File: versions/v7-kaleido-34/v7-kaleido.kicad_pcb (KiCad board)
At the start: 4 copper layers, 138.1 x 104.6 mm, 140 parts, among them J1 USB_C_Receptacle_USB2.0, J10 AXT-310124, J11 THD2528-11SD-GF, J12 SM04B-SRSS-TB_LF__SN_, J2 EXTENSION_HEADER, J3 USB_HDR, J4 Conn_01x08_Pin, J5 CONN_BAT, J6 FH34SRJ-6S-0.5SH_99_, J7 ESP_HDR, J8 ESP_XTR_HDR, J9 Conn_01x08_Pin, Q1 AO3401A, Q3 MMBT3904, Q4 MMBT3904, U1 RT9080-33GJ5, U10 ED060XC5, U11 TP4056, U12 RY3730, U2 PCA9535PW, U3 RSL48_4P4X4P4, U4 USBLC6-2P6, U5 XC6206PxxxMR, U6 RY3730, U7 PCF8563T, U8 ESP32-S3-WROOM-1, U9 CH340C, Y1 32.768K

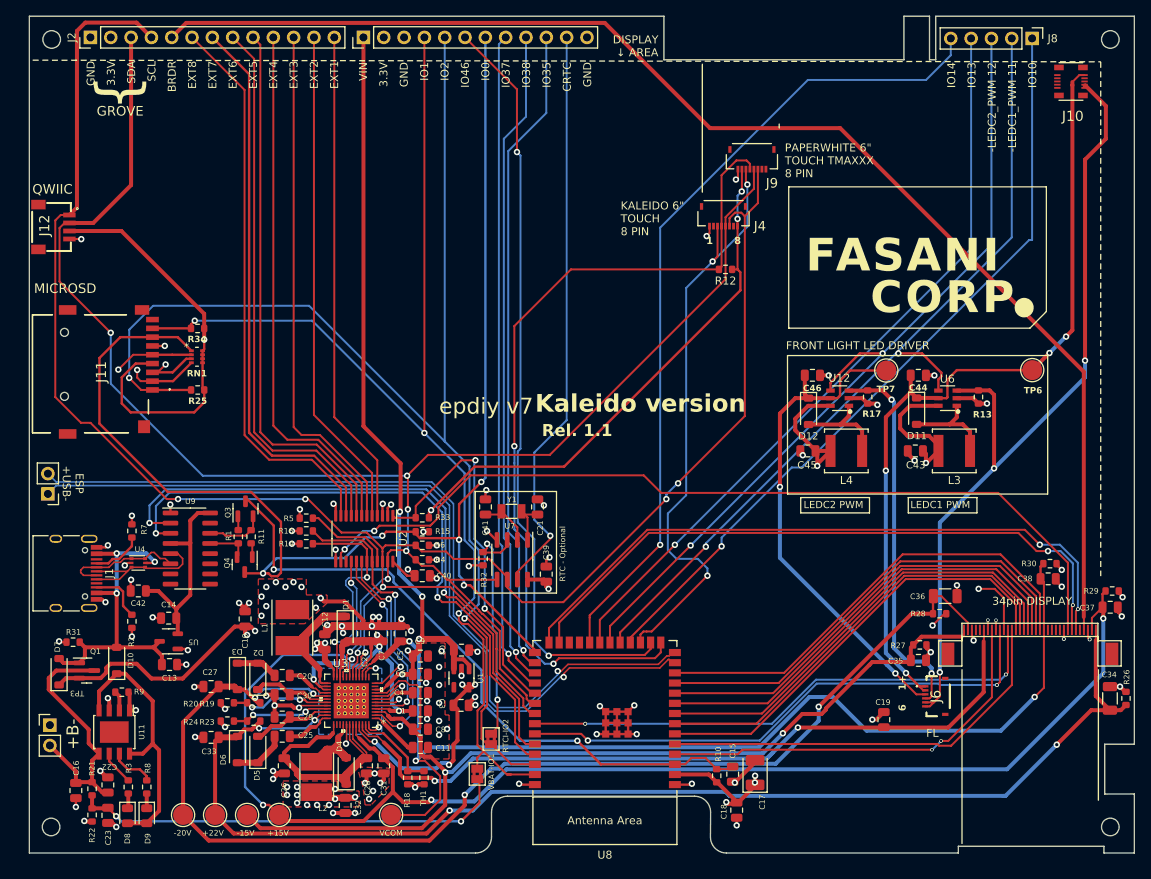
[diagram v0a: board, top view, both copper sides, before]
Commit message: Add kindle 34 pins versions (RAW)
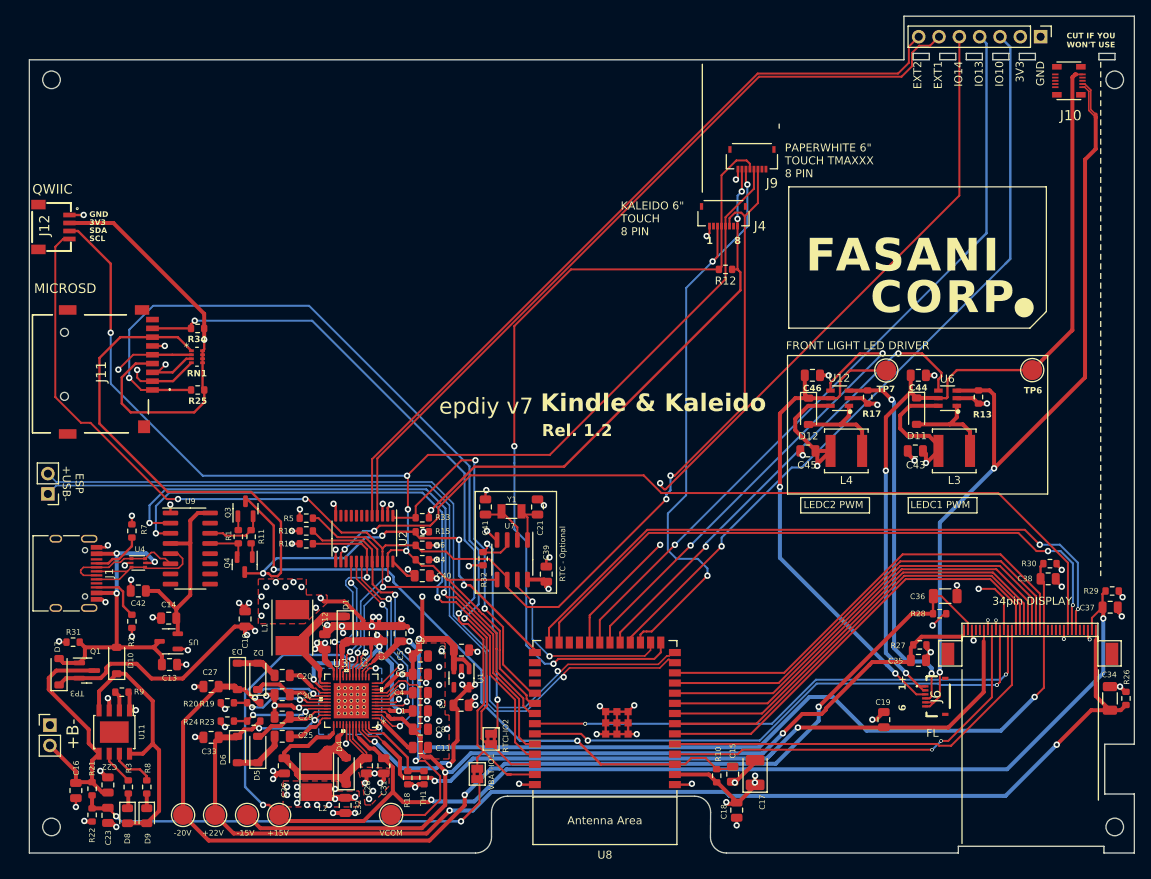
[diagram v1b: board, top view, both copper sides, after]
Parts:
- removed J2: EXTENSION_HEADER, Connector_PinHeader_2.54mm:PinHeader_1x13_P2.54mm_Vertical
- removed J7: ESP_HDR, Connector_PinHeader_2.54mm:PinHeader_1x12_P2.54mm_Vertical
- removed J8: ESP_XTR_HDR, Connector_PinHeader_2.54mm:PinHeader_1x05_P2.54mm_Vertical
- added J102: ESP_XTR_HDR, Connector_PinHeader_2.54mm:PinHeader_1x07_P2.54mm_Vertical, F.Cu at (186.3, 46.6)
- L3, L4: value L -> 22 uH
- R3: value 1k -> 3.8k
- R9: value 6.8k -> 3.8k
- U3: value RSL48_4P4X4P4 -> TPS651851RSLR
- moved H1 5.07 mm to (195.6, 52.0)
- moved H4 5.04 mm to (62.6, 52.0)
- moved H3 0.55 mm to (195.6, 145.3)
- moved J10 0.27 mm to (189.8, 52.1)
- moved H2 0.05 mm to (62.6, 145.3)
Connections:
- C17 pad 1: 3.3V -> +3V3
- C18 pad 2: 3.3V -> +3V3
- C3 pad 2: 3.3V -> +3V3
- C39 pad 2: 3.3V -> +3V3
- C40 pad 1: 3.3V -> +3V3
- J11 pad 4: 3.3V -> +3V3
- J12 pad 1: /SCL -> GND
- J12 pad 2: /SDA -> +3V3
- J12 pad 3: 3.3V -> /SDA
- J12 pad 4: GND -> /SCL
- J4 pad 8: 3.3V -> +3V3
- J9 pad 2: 3.3V -> +3V3
- R10 pad 2: 3.3V -> +3V3
- R12 pad 1: 3.3V -> +3V3
- R14 pad 1: 3.3V -> +3V3
- R15 pad 2: 3.3V -> +3V3
- R16 pad 1: 3.3V -> +3V3
- R25 pad 1: 3.3V -> +3V3
- R32 pad 2: 3.3V -> +3V3
- R33 pad 1: 3.3V -> +3V3
- R34 pad 2: 3.3V -> +3V3
- R4 pad 1: 3.3V -> +3V3
- R6 pad 1: 3.3V -> +3V3
- RN1 pad 5: 3.3V -> +3V3
- RN1 pad 6: 3.3V -> +3V3
- RN1 pad 7: 3.3V -> +3V3
- RN1 pad 8: 3.3V -> +3V3
- U1 pad 5: 3.3V -> +3V3
- U2 pad 10: /EXT7 -> unconnected-(U2-IO0_6-Pad10)
- U2 pad 11: /EXT8 -> unconnected-(U2-IO0_7-Pad11)
- U2 pad 24: 3.3V -> +3V3
- U2 pad 6: /EXT3 -> unconnected-(U2-IO0_2-Pad6)
- U2 pad 7: /EXT4 -> unconnected-(U2-IO0_3-Pad7)
- U2 pad 8: /EXT5 -> unconnected-(U2-IO0_4-Pad8)
- U2 pad 9: /EXT6 -> unconnected-(U2-IO0_5-Pad9)
- U3 pad 45: 3.3V -> +3V3
- U7 pad 8: 3.3V -> +3V3
- U8 pad 16: /GPIO_46 -> /RTC_CLK
- U8 pad 2: 3.3V -> +3V3
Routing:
- net 3.3V: track 310.8 -> 0.00 mm, vias 19 -> 0
- net +3V3: track 0.00 -> 254.0 mm, vias 0 -> 19
- net /BORDER: track 165.1 -> 0.00 mm
- net /GPIO_46: track 95.8 -> 0.00 mm, vias 2 -> 0
- net /GPIO_37: track 83.2 -> 0.00 mm, vias 1 -> 0
- net /GPIO_36: track 82.5 -> 0.00 mm, vias 1 -> 0
- net /GPIO_35: track 81.8 -> 0.00 mm, vias 1 -> 0
- net VIN: track 275.3 -> 202.2 mm, vias 23 -> 22
- net /EXT8: track 70.6 -> 0.00 mm
- net /EXT7: track 69.8 -> 0.00 mm
- net /EXT6: track 69.1 -> 0.00 mm
- net /EXT5: track 68.4 -> 0.00 mm
- net /EXT4: track 66.6 -> 0.00 mm
- net /EXT3: track 64.9 -> 0.00 mm
- net /IO0: track 170.6 -> 106.4 mm, vias 5 -> 4
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- added copper zone on In2.Cu, net +3V3
- removed copper zone on In2.Cu, net 3.3V
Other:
- outline, holes or cut-outs redrawn
- board text added: "3V3"
- board text added: "CUT IF YOU WON'T USE"
- board text added: "Kindle & Kaleido"
- board text added: "Rel. 1.2"
- board text removed: "-LEDC1_PWM 11"
- board text removed: "-LEDC2_PWM 12"
- board text removed: "3.3V"
- board text removed: "BRDR"
- board text removed: "CRTC"
- board text removed: "DISPLAY ↓ AREA"
- board text removed: "EXT3"
- board text removed: "EXT4"
- board text removed: "EXT5"
- board text removed: "EXT6"
- board text removed: "EXT7"
- board text removed: "EXT8"
- board text removed: "GROVE"
- board text removed: "IO0"
- board text removed: "IO1"
- board text removed: "IO2"
- board text removed: "IO35"
- board text removed: "IO37"
- board text removed: "IO38"
- board text removed: "IO46"
- board text removed: "Kaleido version"
- board text removed: "Rel. 1.1"
- board text removed: "VIN"
- board text removed: "{"
